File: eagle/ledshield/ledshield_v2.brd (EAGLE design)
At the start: 42 x 42 mm, 15 parts, among them U3 PCA9685

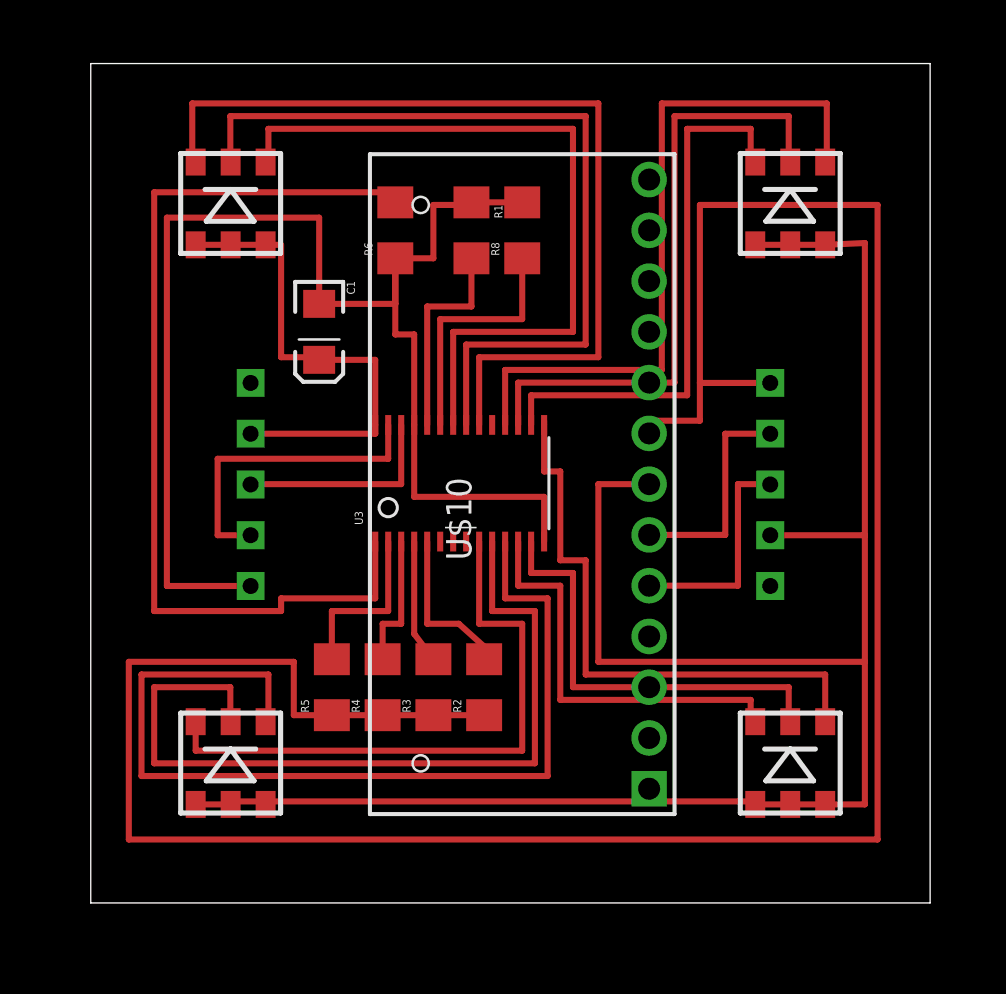
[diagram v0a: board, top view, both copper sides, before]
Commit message: updated led shield design with common ground and passing design and electrical checks also started bluetooth/arduino communication to work in reverse from processing to arduino
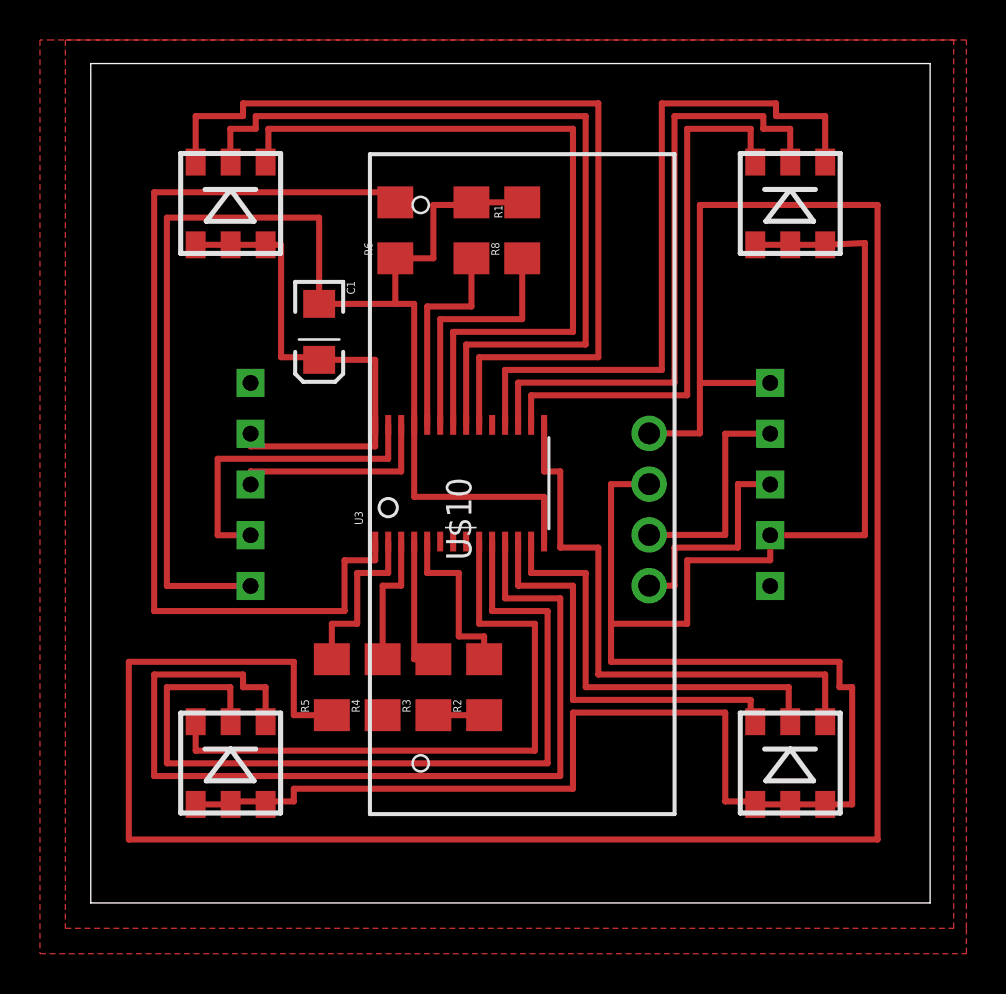
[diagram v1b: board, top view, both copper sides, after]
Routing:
- net +3V3: track 96.9 -> 109.7 mm
- net GND2: track 124.9 -> 119.9 mm
- net GND: track 71.4 -> 69.1 mm
- net PWM3: track 30.4 -> 31.7 mm
- net 3.3V: track 24.7 -> 25.9 mm
- net A4: track 8.03 -> 8.74 mm
- net A3: track 6.21 -> 6.85 mm
- added copper zone on layer 1, net GND
- added copper zone on layer 1, net GND2
